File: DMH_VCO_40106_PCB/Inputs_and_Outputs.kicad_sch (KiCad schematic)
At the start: 13 parts, among them J1 TS_Jack_6.35mm_Sw, J150 Conn_01x12, J2 TS_Jack_6.35mm_Sw, J200 IDC_02x05, J3 TS_Jack_6.35mm_Sw, J4 TS_Jack_6.35mm_Sw, J5 TS_Jack_6.35mm_Sw, J6 TS_Jack_6.35mm_Sw, J7 TS_Jack_6.35mm_Sw, J8 TS_Jack_6.35mm_Sw, J9 TS_Jack_6.35mm_Sw, SW1 SW_SPDT_321_OnOff, SW2 SW_SPDT_321_OnOff

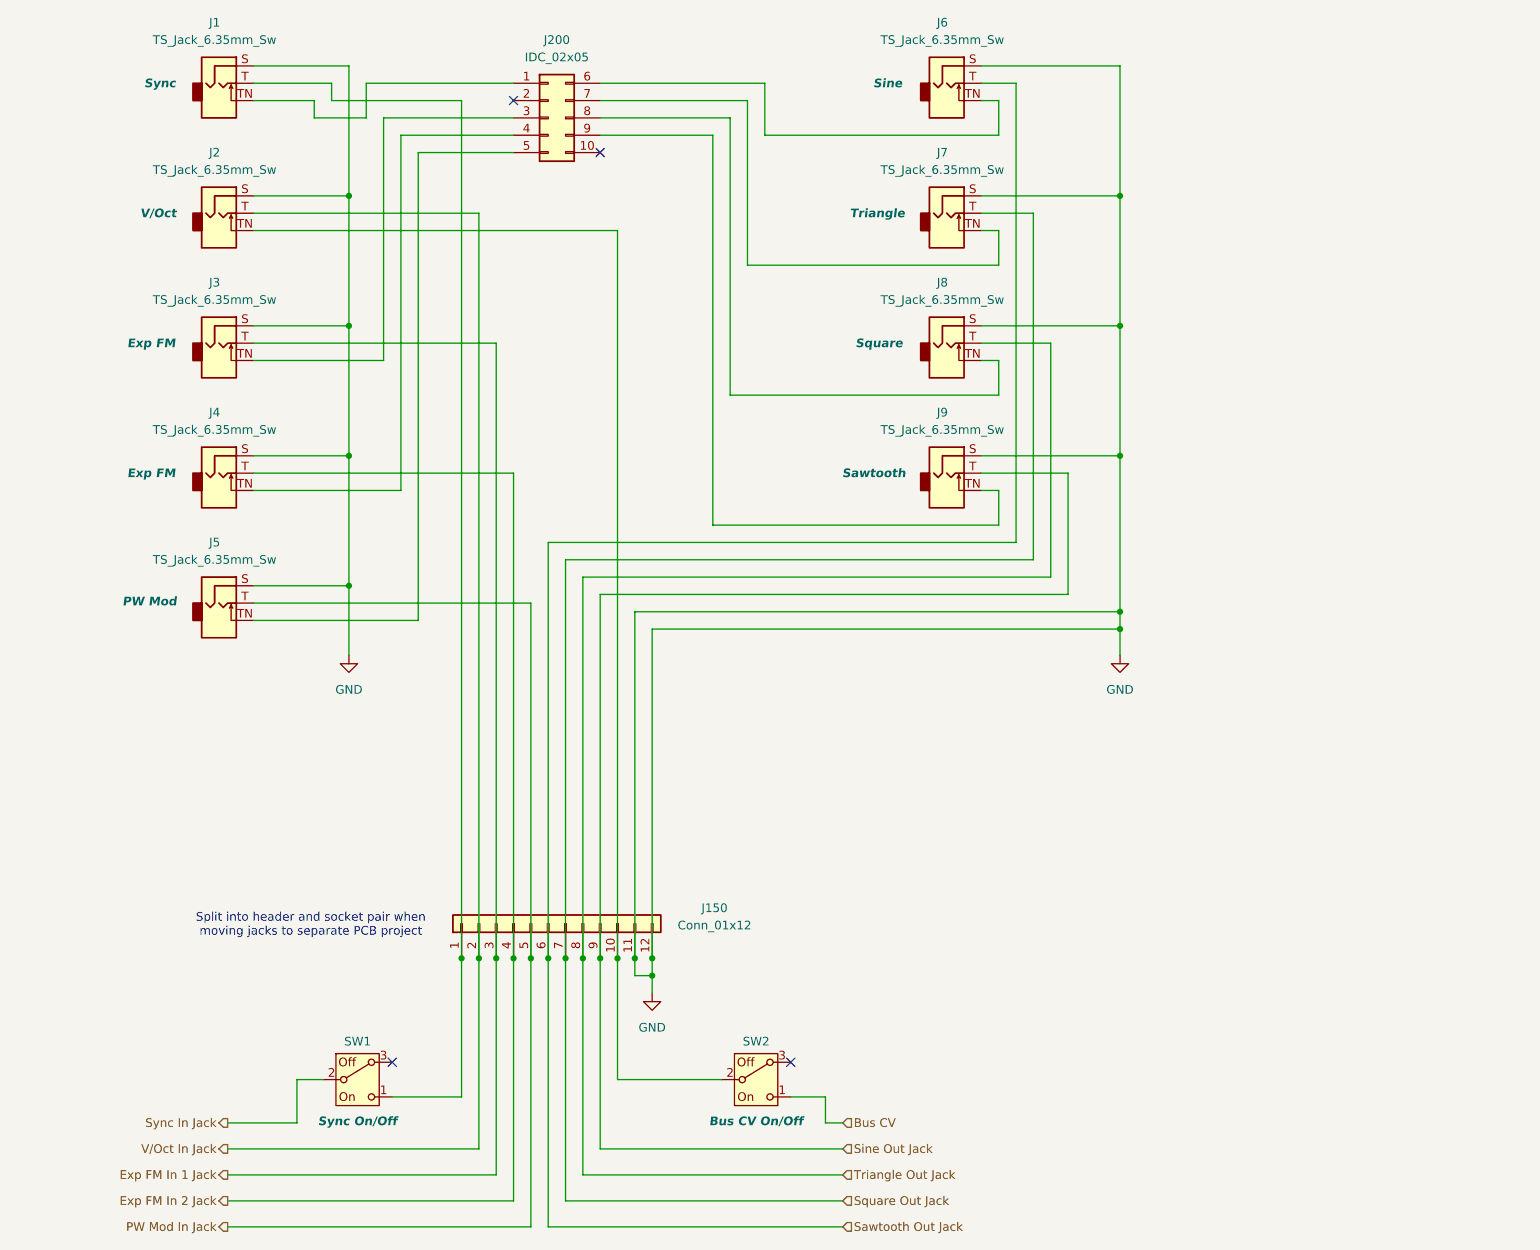
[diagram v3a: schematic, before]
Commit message: Started positioning components on PCB
Moving some input resistores from main PCB to Jacks PCB
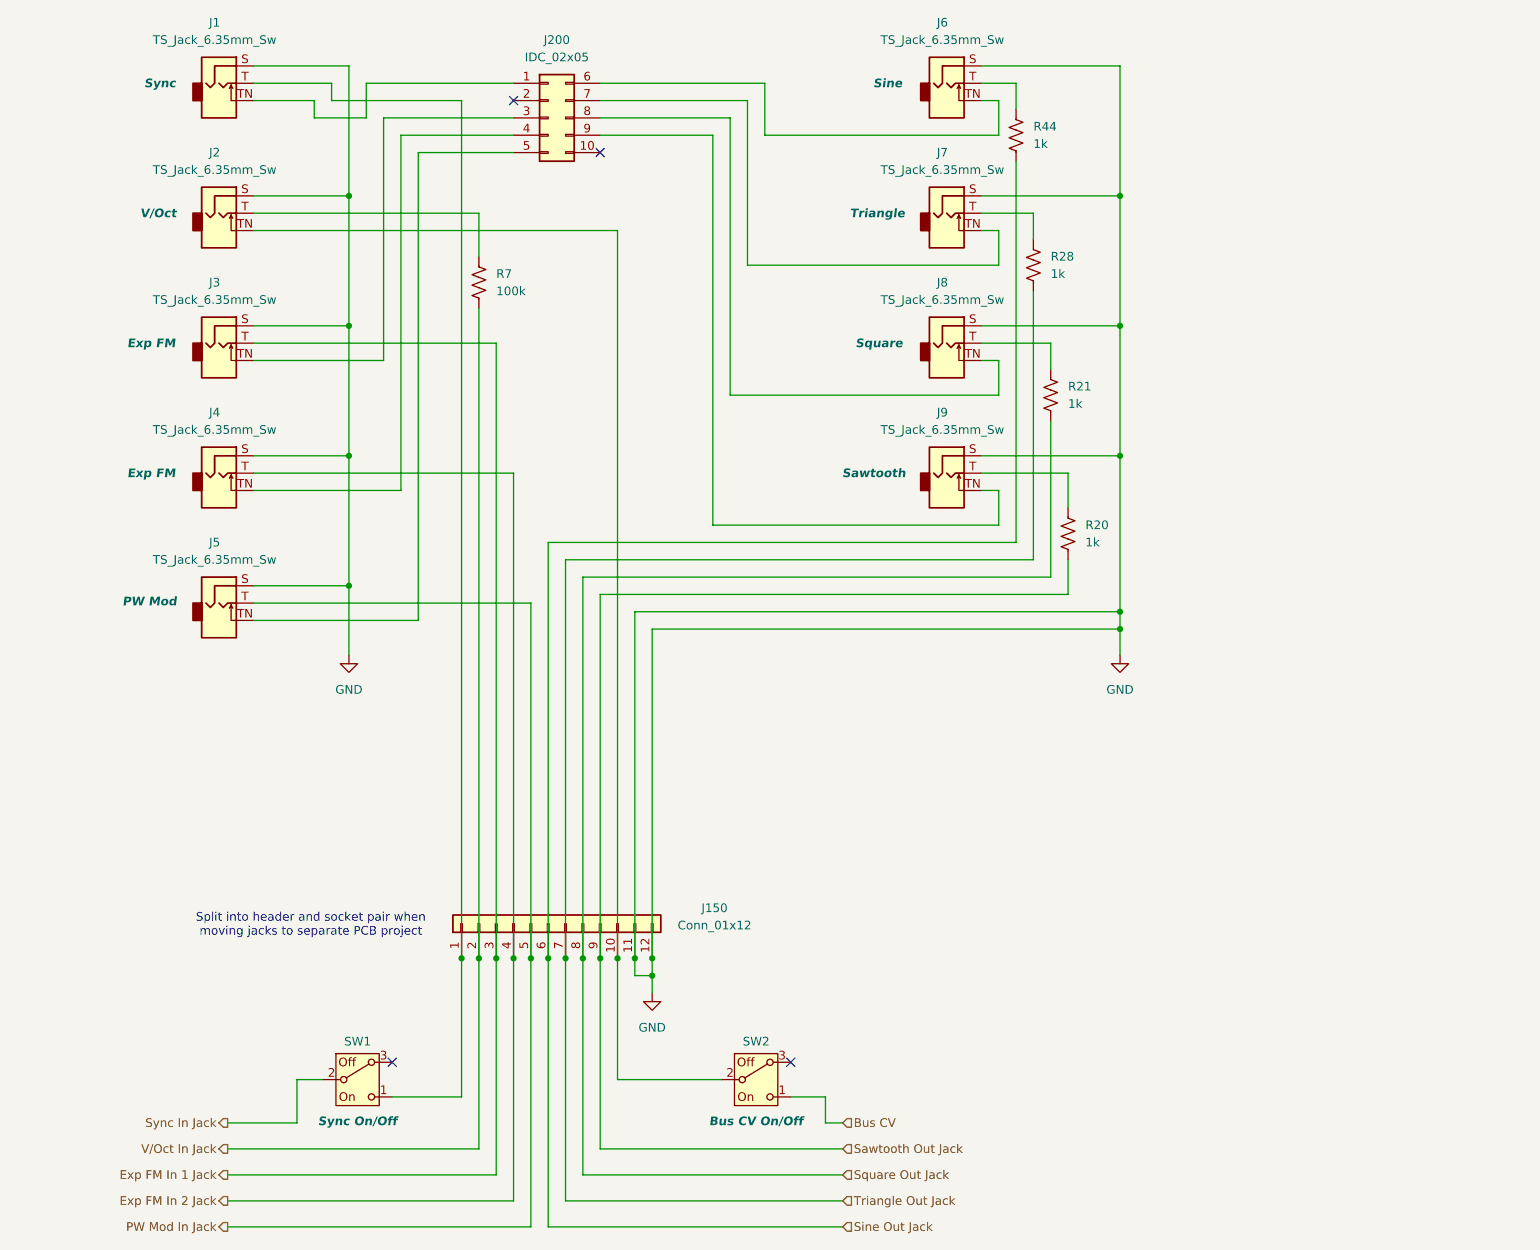
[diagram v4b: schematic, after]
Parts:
- added R20, R21, R28, R44: 1k, Resistor_THT:R_Axial_DIN0207_L6.3mm_D2.5mm_P7.62mm_Horizontal, symbol Device:R_US
- added R7: 100k, Resistor_THT:R_Axial_DIN0207_L6.3mm_D2.5mm_P7.62mm_Horizontal, symbol Device:R_US
- SW1, SW2: footprint (none) -> SynthStuff:Toggle_Switch_THT
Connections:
- net Sawtooth Out Jack: now also J150.9 (Pin_9), R20.2; no longer J150.6 (Pin_6), J6.T
- net Sine Out Jack: now also J150.6 (Pin_6), R44.1; no longer J150.9 (Pin_9), J9.T
- net Square Out Jack: now also J150.8 (Pin_8), R21.2; no longer J150.7 (Pin_7), J7.T
- net Triangle Out Jack: now also J150.7 (Pin_7), R28.1; no longer J150.8 (Pin_8), J8.T
- net V/Oct In Jack: now also R7.1; no longer J2.T
- new net: J9.T, R20.1
- new net: J2.T, R7.2
- new net: J6.T, R44.2
- new net: J7.T, R28.2
- new net: J8.T, R21.1
